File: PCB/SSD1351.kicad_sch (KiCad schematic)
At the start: 18 parts, among them J1 Conn_01x07

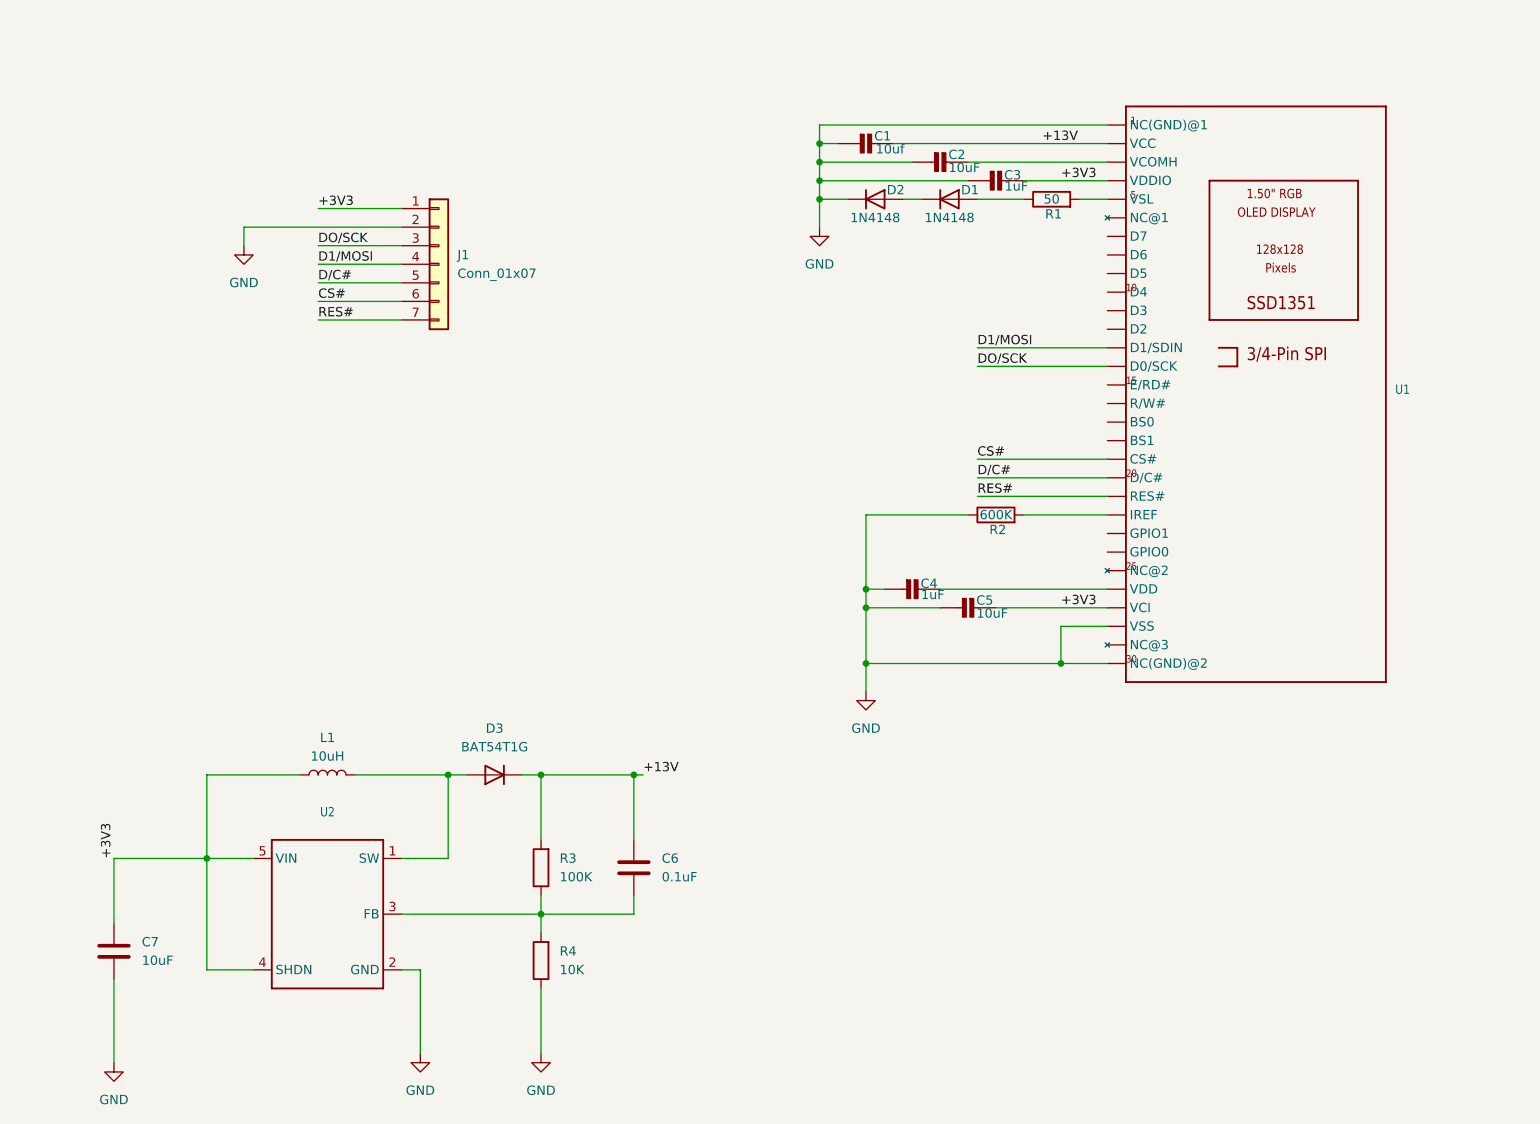
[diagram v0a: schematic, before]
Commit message: Added SKUs for components
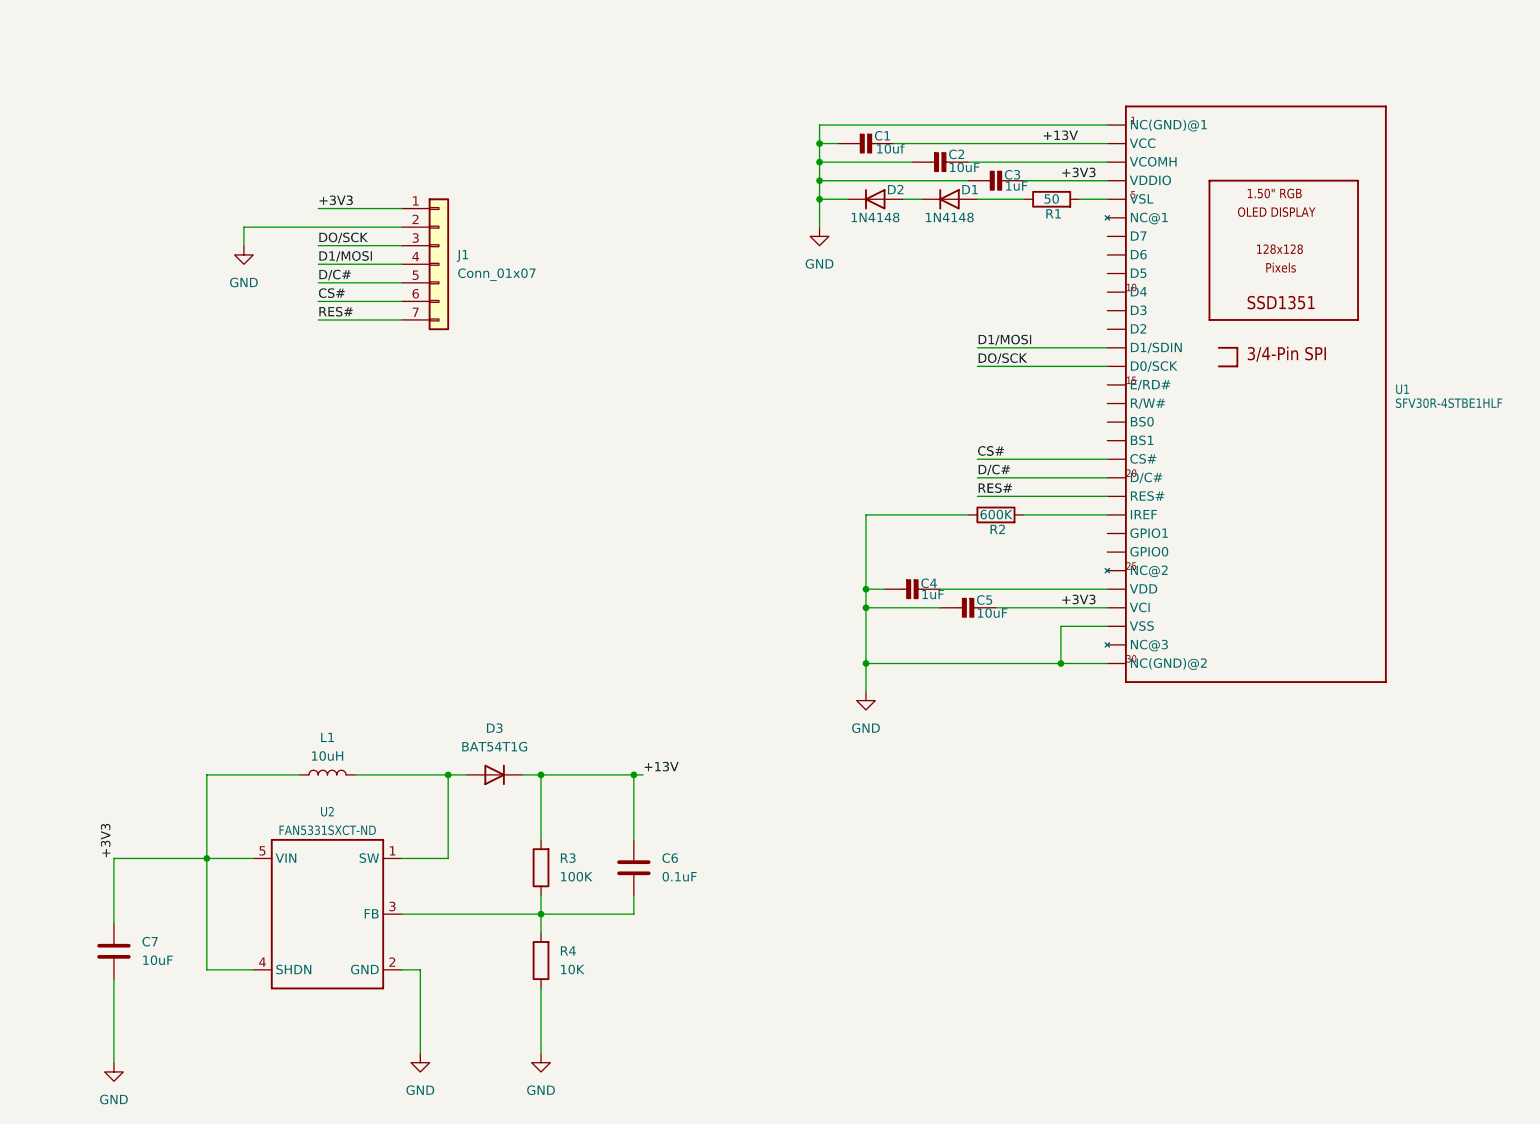
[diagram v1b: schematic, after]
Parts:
- U1: value ~ -> SFV30R-4STBE1HLF
- U2: value ~ -> FAN5331SXCT-ND
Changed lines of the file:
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@@
 			)
 		)
-		(property "Value" "~"
+		(property "Value" "FAN5331SXCT-ND"
 			(at 67.31 127 0)
 			(effects
@@
 			)
 		)
-		(property "Value" "~"
+		(property "Value" "SFV30R-4STBE1HLF"
 			(at 213.36 68.58 0)
 			(effects

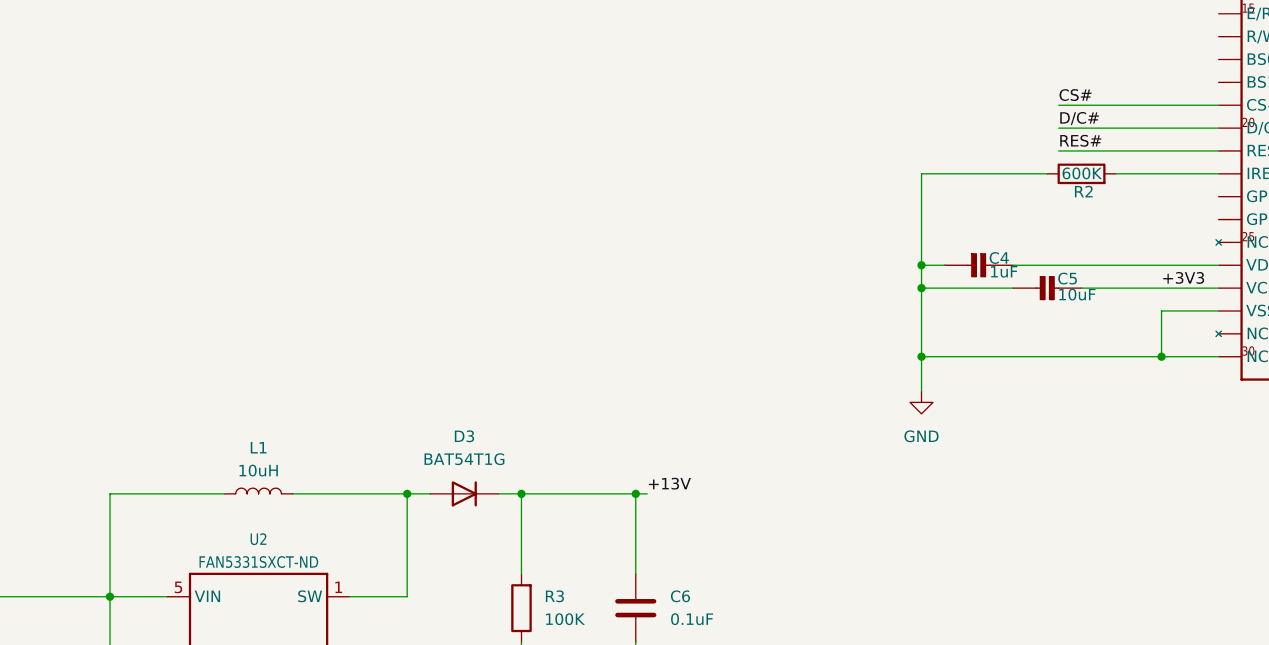
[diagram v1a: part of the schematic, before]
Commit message: Adding a few more SKUs
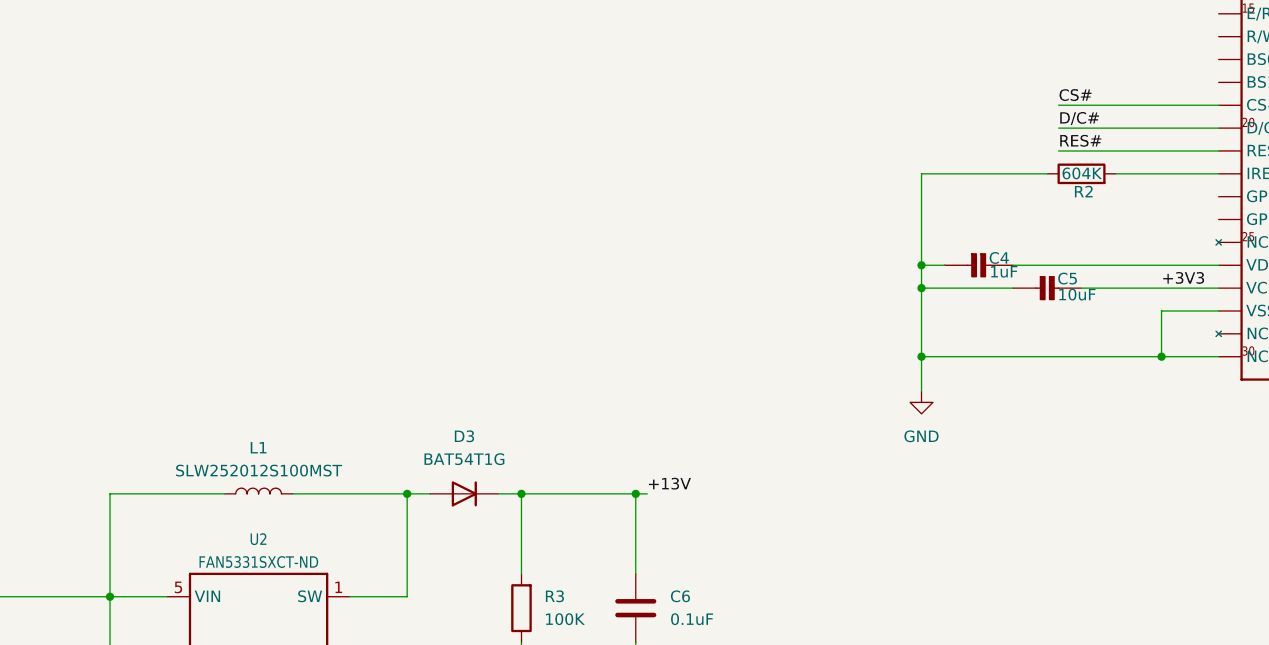
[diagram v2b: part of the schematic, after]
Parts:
- L1: value 10uH -> SLW252012S100MST
- R2: value 600K -> 604K
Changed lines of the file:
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@@
 			)
 		)
-		(property "Value" "10uH"
+		(property "Value" "SLW252012S100MST"
 			(at 67.31 116.84 90)
 			(effects
@@
 			)
 		)
-		(property "Value" "600K"
+		(property "Value" "604K"
 			(at 158.75 83.82 90)
 			(effects

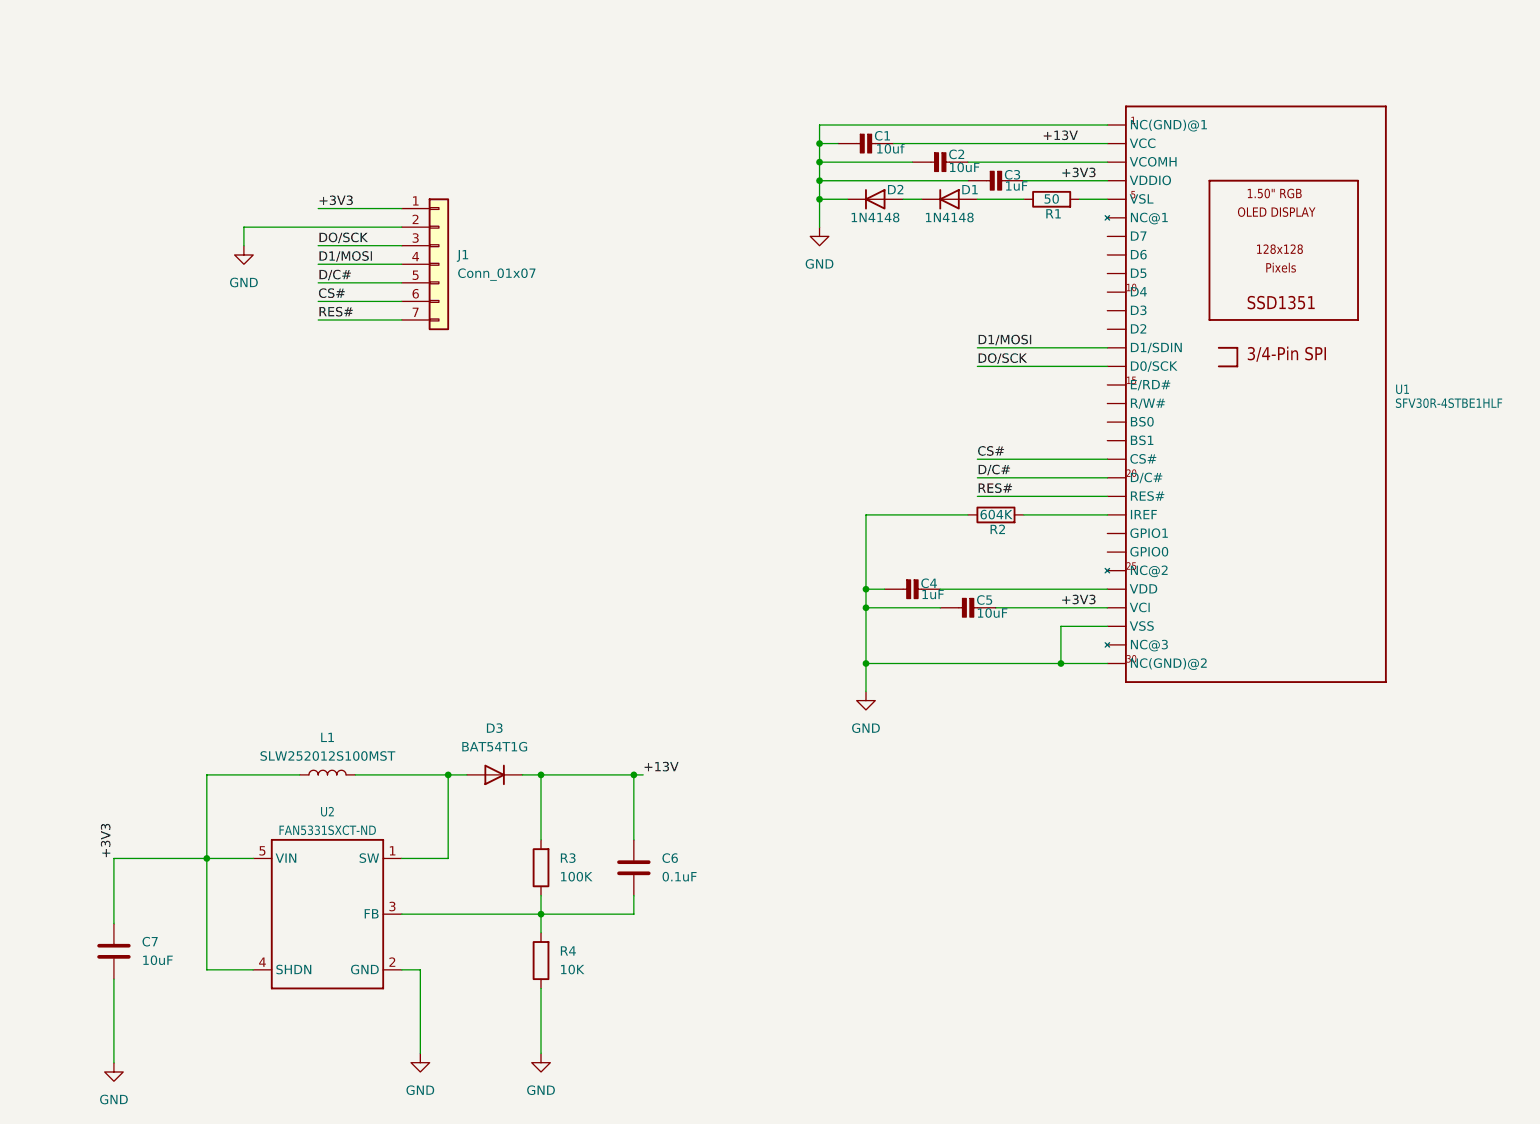
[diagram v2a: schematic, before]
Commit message: Updated PCB
Consulted datasheets and adjusted cap ratings.
Reworked power distribution and location.
Started tracking down specific components and updating the BOM.
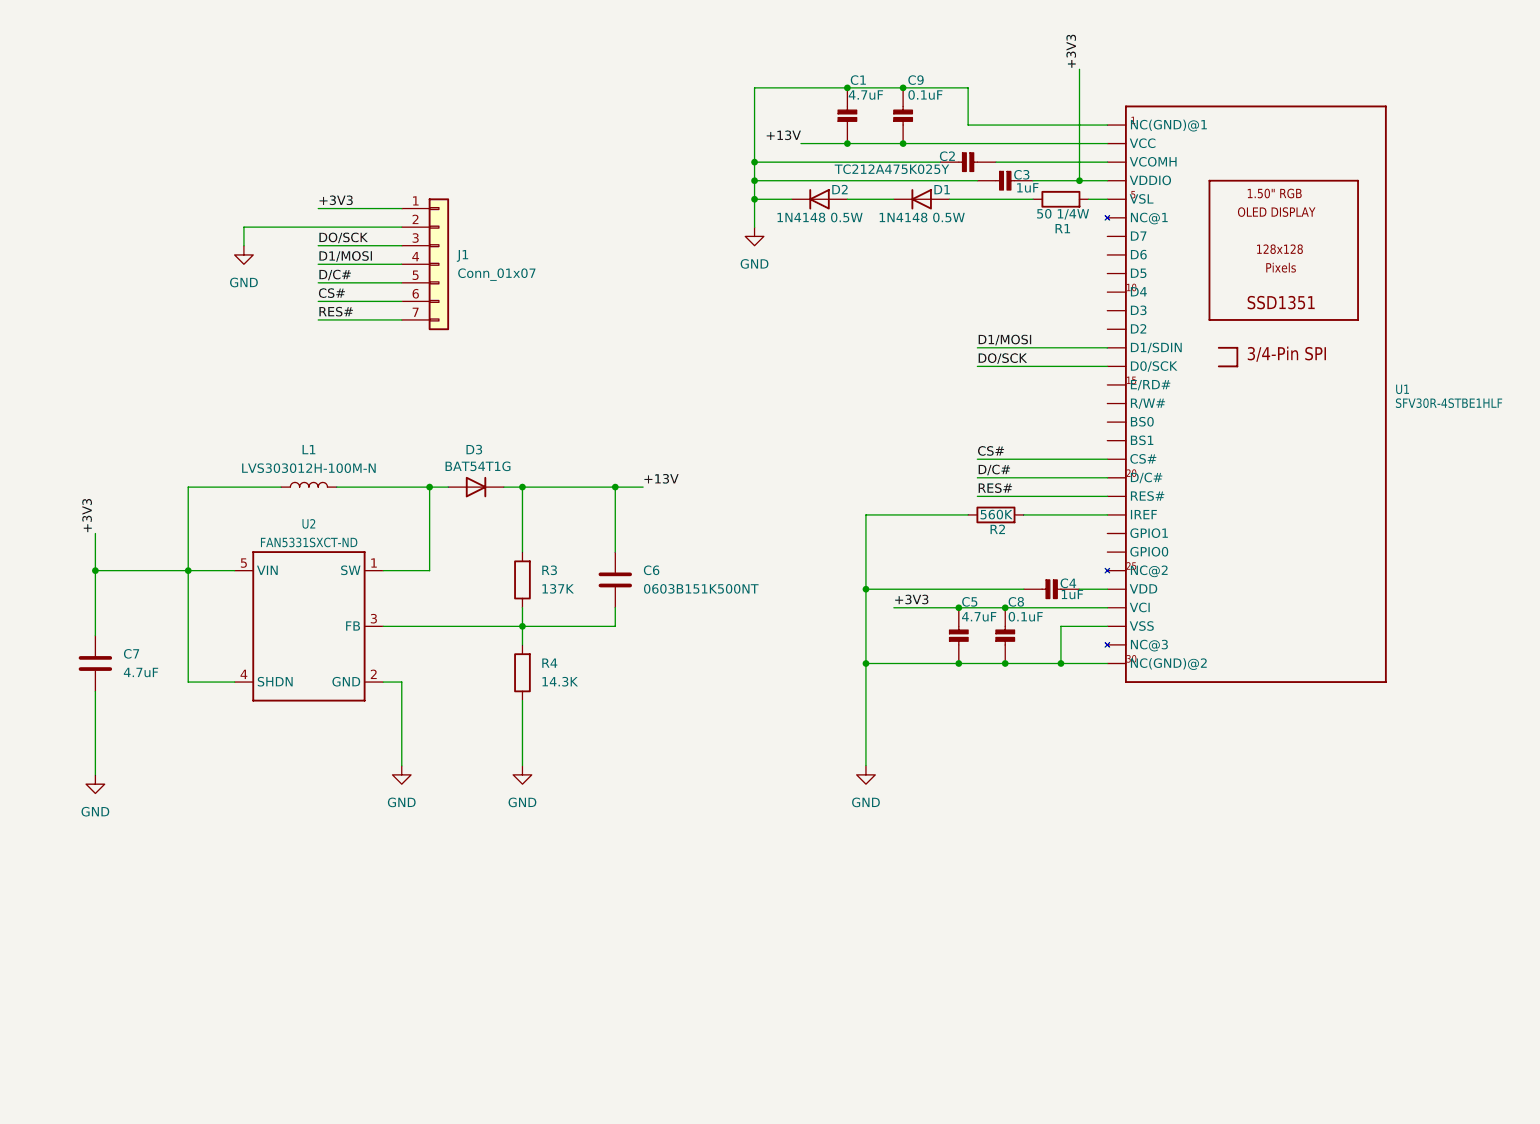
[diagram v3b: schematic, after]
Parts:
- added C8, C9: 0.1uF, Capacitor_SMD:C_0603_1608Metric, symbol SSD1351:CAP_CERAMIC_0805
- C1: value 10uf -> 4.7uF
- C2: value 10uF -> TC212A475K025Y; footprint Capacitor_SMD:C_0805_2012Metric -> Capacitor_Tantalum_SMD:CP_EIA-3216-18_Kemet-A
- C5, C7: value 10uF -> 4.7uF
- C6: value 0.1uF -> 0603B151K500NT
- D1, D2: value 1N4148 -> 1N4148 0.5W
- L1: value SLW252012S100MST -> LVS303012H-100M-N; footprint Inductor_SMD:L_1008_2520Metric_Pad1.43x2.20mm_HandSolder -> Inductor_SMD:L_Sunlord_SWPA3012S
- R1: value 50 -> 50 1/4W
- R2: value 604K -> 560K
- R3: value 100K -> 137K
- R4: value 10K -> 14.3K
- U2: footprint SSD1351:SOT23-5 -> Package_TO_SOT_SMD:SOT-23-5_HandSoldering
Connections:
- net +13V: now also C1.2 (P$2), C9.2 (P$2); no longer C1.1 (P$1)
- net +3V3: now also C8.1 (P$1)
- net GND: now also C1.1 (P$1), C8.2 (P$2), C9.1 (P$1); no longer C1.2 (P$2)
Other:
- moved on the sheet: C1, C2, C3, C4, C5, C6, C7, D1, D2, D3, L1, R1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
